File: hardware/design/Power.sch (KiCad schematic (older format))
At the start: 12 parts

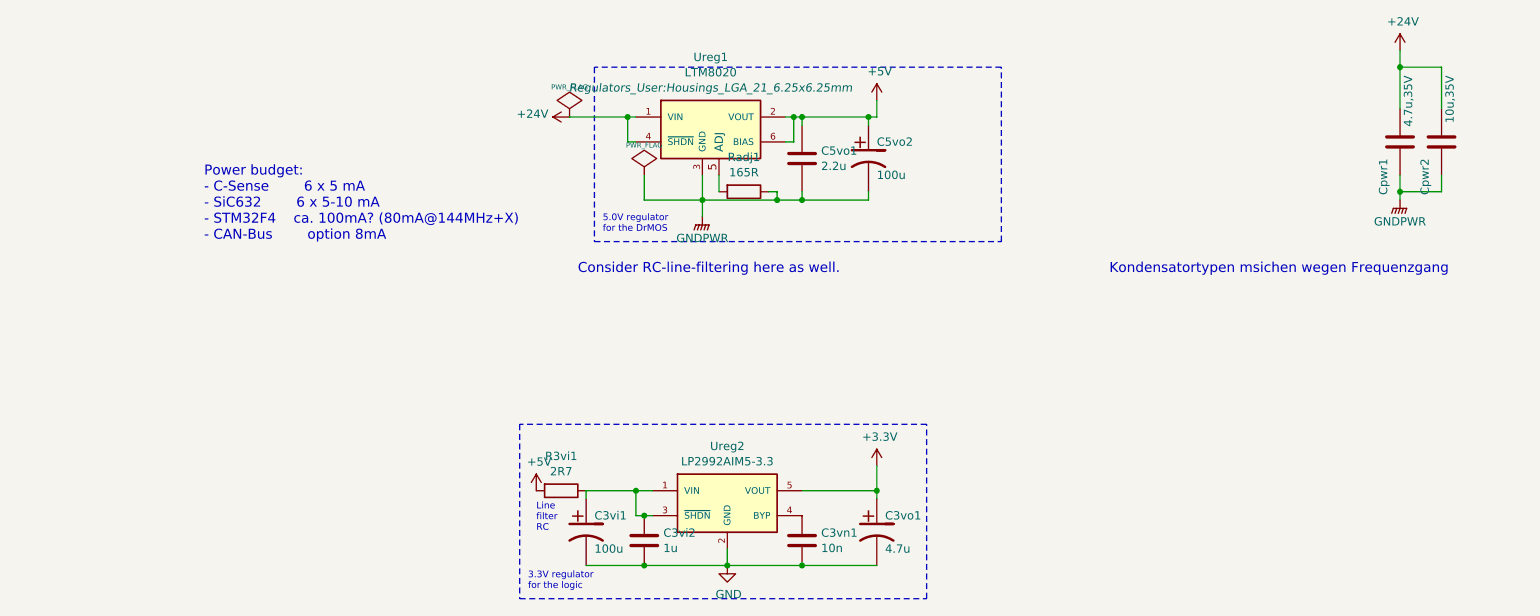
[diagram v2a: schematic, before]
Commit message: Added a few caps on the back next to the DrMOS
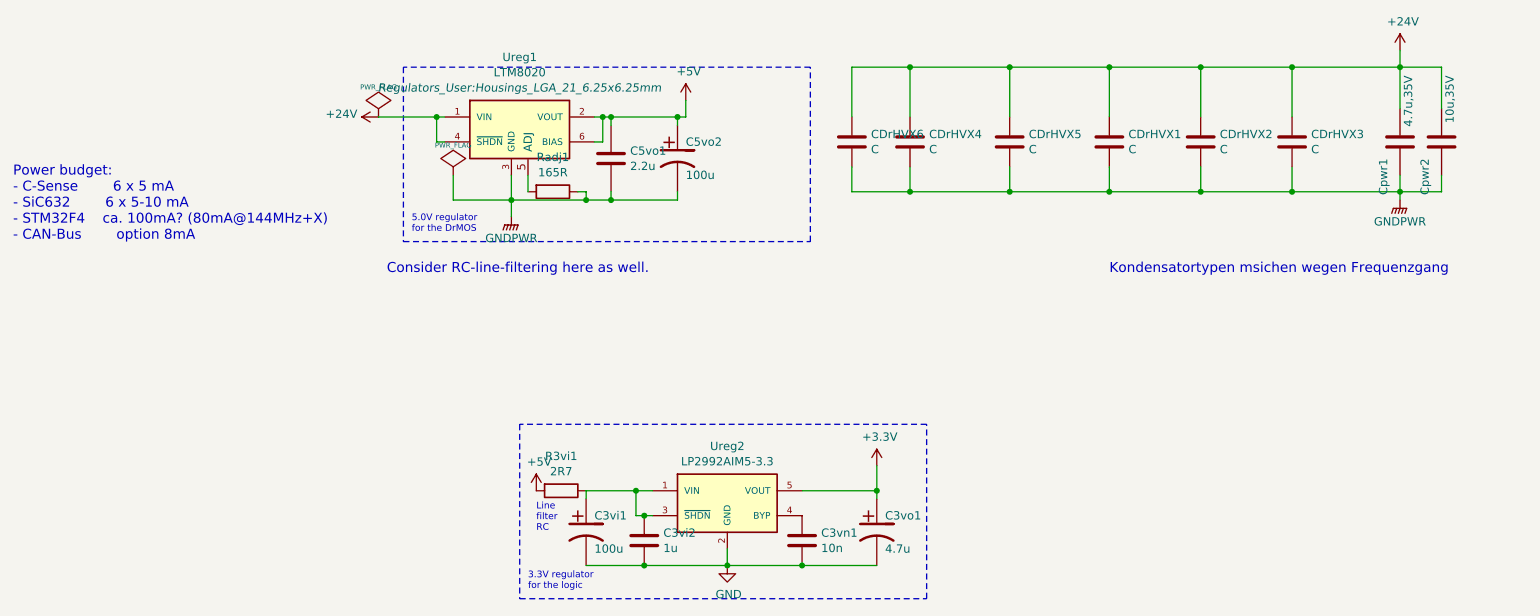
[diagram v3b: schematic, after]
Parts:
- added CDrHVX1, CDrHVX2, CDrHVX3, CDrHVX4, CDrHVX5, CDrHVX6: C, Capacitors_SMD:C_1206, symbol C
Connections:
- net +24V: now also CDrHVX1.1, CDrHVX2.1, CDrHVX3.1, CDrHVX4.1, CDrHVX5.1, CDrHVX6.1
- net GNDPWR: now also CDrHVX1.2, CDrHVX2.2, CDrHVX3.2, CDrHVX4.2, CDrHVX5.2, CDrHVX6.2
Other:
- moved on the sheet: C5vo1, C5vo2, Radj1, Ureg1

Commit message: Same.
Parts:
- Ureg1: Manufacturer (none) -> Linear Technology; Part Number (none) -> LTM8020V
- Ureg2: Manufacturer (none) -> Texas Instruments; Part Number (none) -> LP2992AIM5-3.3/NOPB
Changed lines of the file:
@@
 00 FD 87 A8 17 00 00 00 00 F4 1F A2 5E 00 00 00 00 D0 7F 88 7A 01 00 00 00 40 FF 21 EA 05 00 00
 00 00 FD 87 A8 17 00 00 00 00 F4 1F A2 5E 00 00 00 00 D0 7F 88 7A 01 00 00 00 40 FF 21 EA 05 00
-00 00 00 FD F7 3F 90 37 91 24 49 74 FD E2 00 00 00 00 49 45 4E 44 AE 42 60 82 00
+00 00 00 FD F7 3F 90 37 91 24 49 74 FD E2 00 00 00 00 49 45 4E 44 AE 42 60 82 02
 EndData
 $EndBitmap
@@
 AB D8 39 0B 59 91 9E DF A8 2A 5B EE 54 3A FD 71 ED 71 2F 29 C3 82 EC 80 87 06 6E C3 98 10 30 3B
 62 9A BB 2D 03 B8 C4 64 FC B5 26 AC 13 9B D1 39 40 41 C1 D6 78 4C 84 BF 94 F0 6F E1 BF 96 F0 0F
-FF 77 E2 FF 1F 0F 43 55 32 21 1C 08 16 00 00 00 00 49 45 4E 44 AE 42 60 82 0E
+FF 77 E2 FF 1F 0F 43 55 32 21 1C 08 16 00 00 00 00 49 45 4E 44 AE 42 60 82 95
 EndData
 $EndBitmap
@@
 F 1 "LP2992AIM5-3.3" H 6350 3676 50  0000 C CNN
 F 2 "TO_SOT_Packages_SMD:SOT-23-5" H 6350 3676 50  0001 C CIN
-F 3 "" H 6350 3450 50  0000 C CNN
+F 3 "http://www.ti.com/lit/ds/symlink/lp2992.pdf" H 6350 3450 50  0001 C CNN
+F 4 "Texas Instruments" H 6350 3450 60  0001 C CNN "Manufacturer"
+F 5 "LP2992AIM5-3.3/NOPB" H 6350 3450 60  0001 C CNN "Part Number"
 	1    6350 3450
 	1    0    0    -1
@@
 F 0 "Ureg1" H 5100 1610 50  0000 C CNN
 F 1 "LTM8020" H 5100 1518 50  0000 C CNN
-F 2 "Regulators_User:Housings_LGA_21_6.25x6.25mm" H 5100 1426 50  0000 C CIN
-F 3 "" H 5100 1200 50  0000 C CNN
+F 2 "Regulators_User:Housings_LGA_21_6.25x6.25mm" H 5100 1426 50  0001 C CIN
+F 3 "http://cds.linear.com/docs/en/datasheet/8020fd.pdf" H 5100 1200 50  0001 C CNN
+F 4 "Linear Technology" H 5100 1200 60  0001 C CNN "Manufacturer"
+F 5 "LTM8020V" H 5100 1200 60  0001 C CNN "Part Number"
 	1    5100 1200
 	1    0    0    -1
